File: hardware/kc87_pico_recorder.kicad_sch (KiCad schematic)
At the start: 8 parts, among them J1 DIN-5_180degree, U1 LM293P

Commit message: Refactor project structure: replace main.c with kc87_pico_recorder.c, update CMakeLists.txt, and add config.h for GPIO configuration
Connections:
- net KC87_REC_PICO: now also A1.4 (GPIO2); no longer A1.14 (GPIO10)
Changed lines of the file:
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@@
 	(wire
 		(pts
-			(xy 167.64 100.33) (xy 170.18 100.33)
+			(xy 166.37 80.01) (xy 170.18 80.01)
 		)
 		(stroke
@@
 	(global_label "KC87_REC_PICO"
 		(shape input)
-		(at 167.64 100.33 180)
+		(at 166.37 80.01 180)
 		(fields_autoplaced yes)
 		(effects
@@
 		)
 		(property "Intersheetrefs" "${INTERSHEET_REFS}"
-			(at 149.5963 100.33 0)
+			(at 148.3263 80.01 0)
 			(effects
 				(font

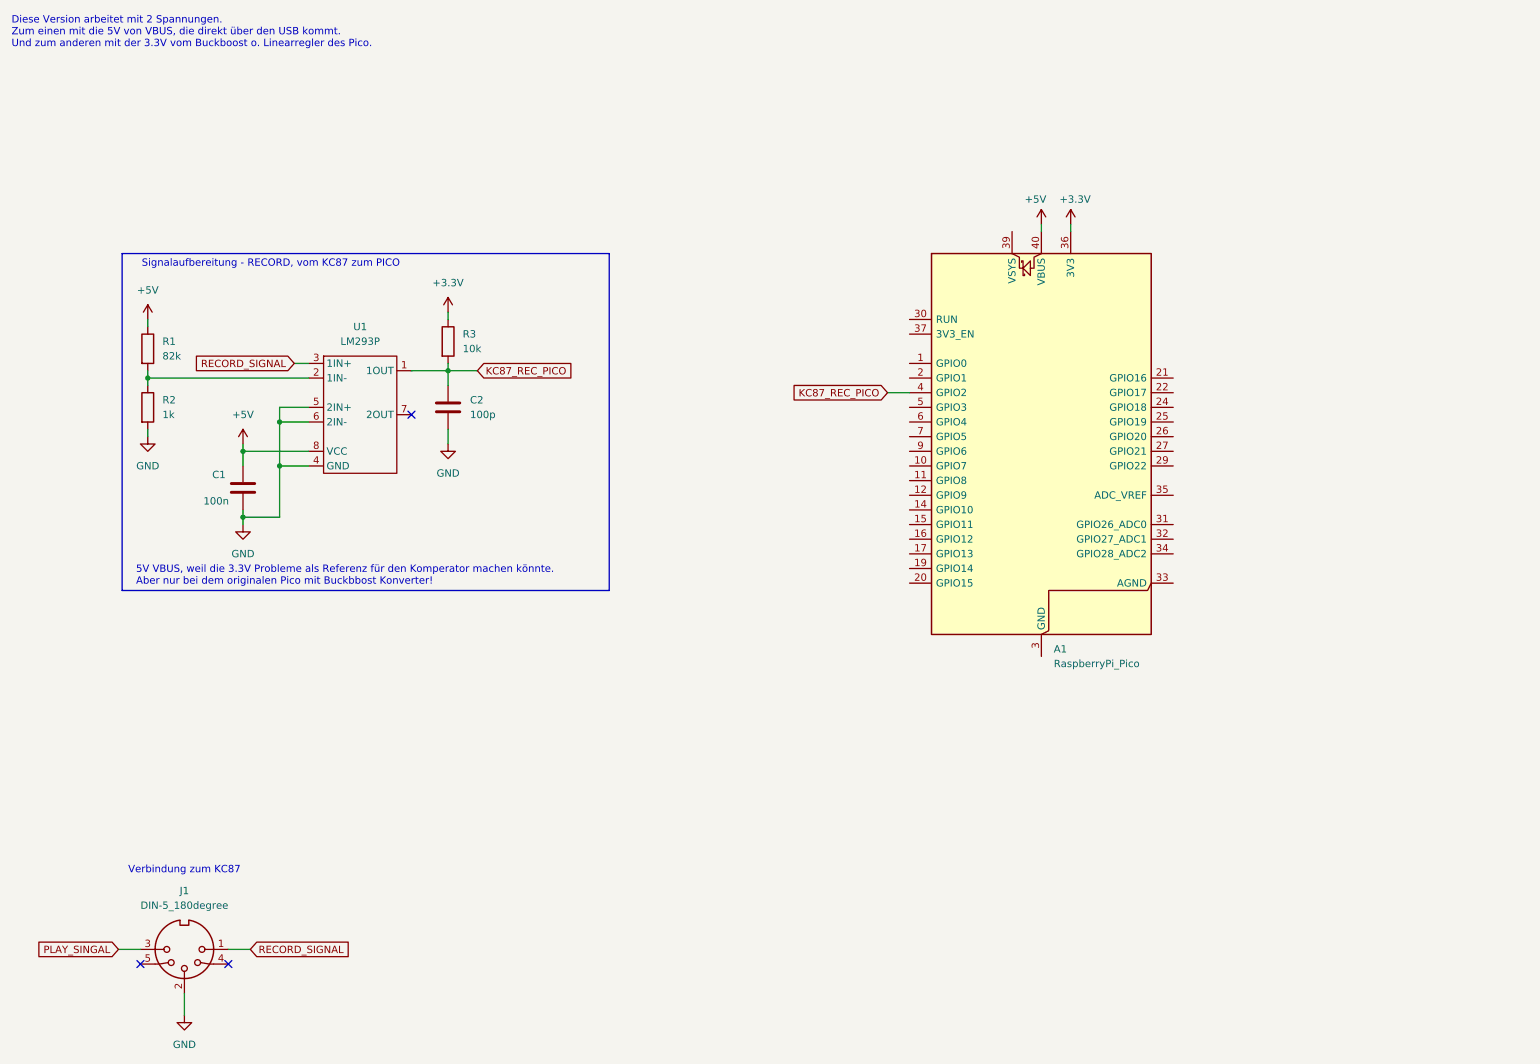
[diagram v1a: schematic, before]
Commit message: Hardware: change kc87_pico_recorder.kicad_sch (new amplifier)
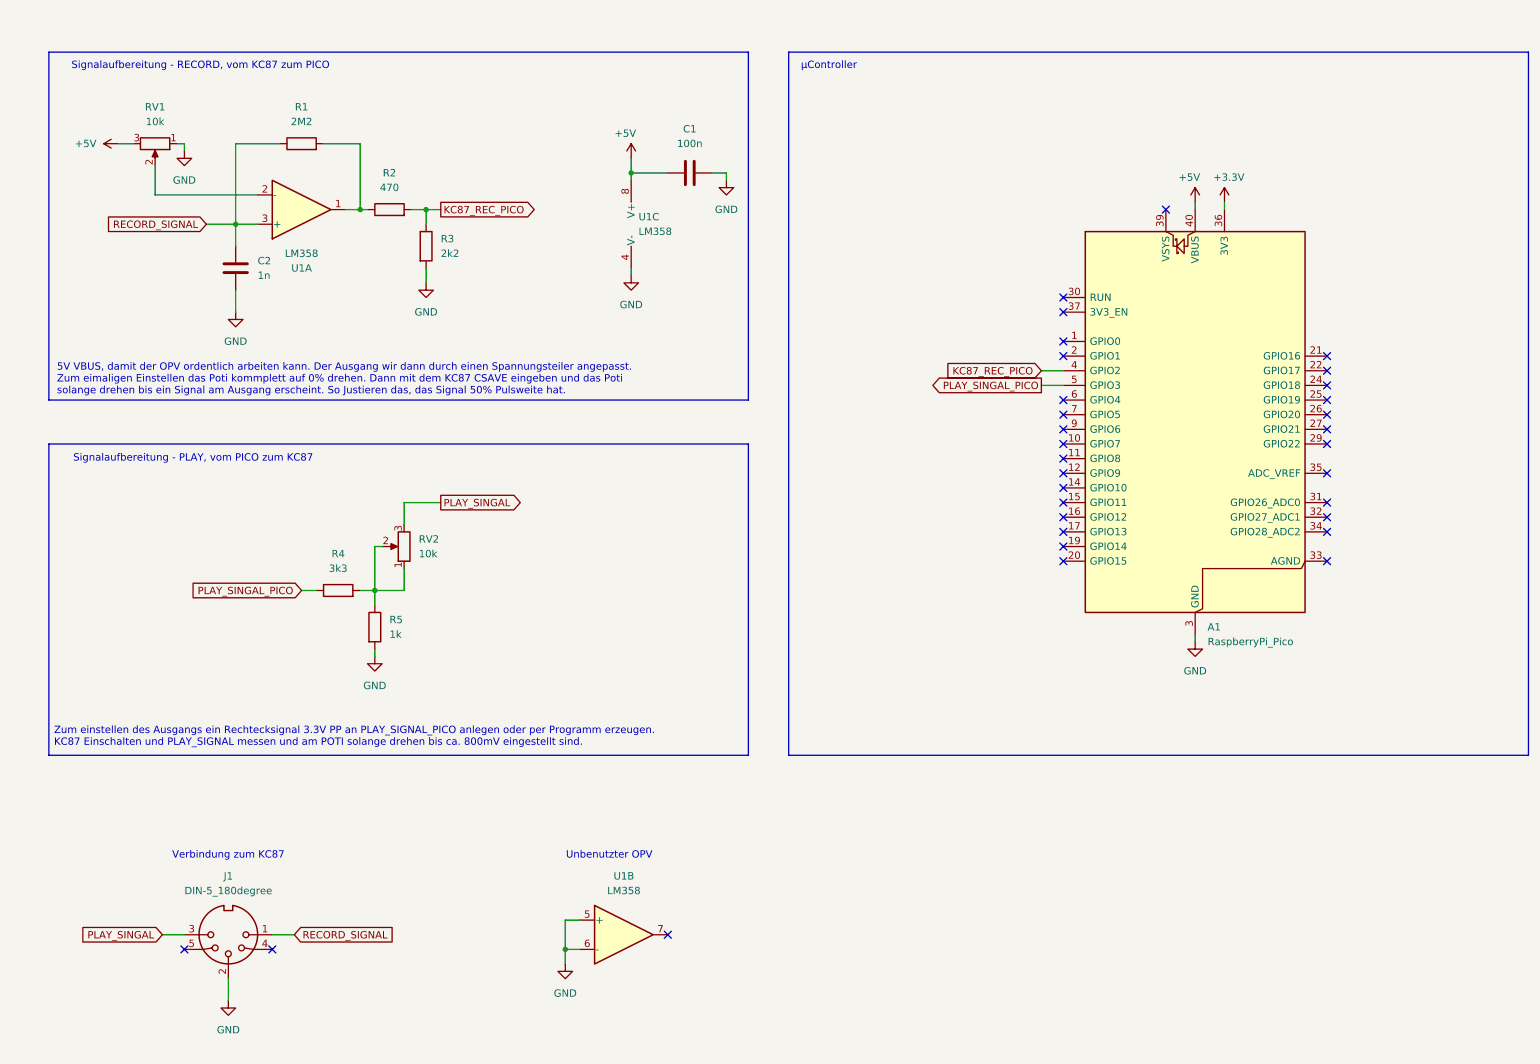
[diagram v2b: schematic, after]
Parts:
- removed U1: LM293P, Package_DIP:DIP-8_W7.62mm_SMDSocket_SmallPads, symbol ic_tk:LM293P
- added R4: 3k3, symbol Device:R
- added R5: 1k, symbol Device:R
- added RV1, RV2: 10k, symbol Device:R_Potentiometer
- added U1: LM358, symbol Amplifier_Operational:LM358
- C2: value 100p -> 1n; footprint Capacitor_SMD:C_0805_2012Metric_Pad1.18x1.45mm_HandSolder -> (none)
- R1: value 82k -> 2M2; footprint Resistor_SMD:R_0805_2012Metric_Pad1.20x1.40mm_HandSolder -> (none)
- R2: value 1k -> 470; footprint Resistor_SMD:R_0805_2012Metric_Pad1.20x1.40mm_HandSolder -> (none)
- R3: value 10k -> 2k2; footprint Resistor_SMD:R_0805_2012Metric_Pad1.20x1.40mm_HandSolder -> (none)
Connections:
- net +3.3V: no longer R3.1
- net +5V: now also RV1.3, U1.8 (V+); no longer R1.1
- net GND: now also A1.13 (GND), A1.18 (GND), A1.23 (GND), A1.28 (GND), A1.3 (GND), A1.38 (GND), A1.8 (GND), R3.2, R5.2, RV1.1, U1.4 (V-), U1.5 (+), U1.6 (-); no longer R2.2
- net KC87_REC_PICO: now also R2.2, R3.1; no longer C2.1, R3.2
- net PLAY_SINGAL: now also RV2.3
- net RECORD_SIGNAL: now also C2.1, R1.1, U1.3 (+)
- net at R1.2, R2.1: now also U1.1
- net PLAY_SINGAL_PICO: now reaches A1.5 (GPIO3)
- net PLAY_SINGAL_PICO: now also R4.1
- new net: R4.2, R5.1, RV2.1, RV2.2
- new net: RV1.2, U1.2 (-)
- no-connect marks 3 -> 32
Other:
- note added: "5V VBUS, damit der OPV ordentlich arbeiten kann. Der Ausgang wir dann durch einen Spannungsteiler angepasst. Zum eimaligen Einstellen das Poti kommplett auf 0% drehen. Dann mit dem KC87 CSAVE eingeben und das Poti solange drehen bis ein Signal am Ausgang erscheint. So Justieren das, das Signal 50% Pulsweite hat."
- note added: "Signalaufbereitung - PLAY, vom PICO zum KC87"
- note added: "Unbenutzter OPV"
- note added: "Zum einstellen des Ausgangs ein Rechtecksignal 3.3V PP an PLAY_SIGNAL_PICO anlegen oder per Programm erzeugen. KC87 Einschalten und PLAY_SIGNAL messen und am POTI solange drehen bis ca. 800mV eingestellt sind."
- note added: "µController"
- note removed: "5V VBUS, weil die 3.3V Probleme als Referenz für den Komperator machen könnte. Aber nur bei dem originalen Pico mit Buckbbost Konverter!"
- note removed: "Diese Version arbeitet mit 2 Spannungen. Zum einen mit die 5V von VBUS, die direkt über den USB kommt. Und zum anderen mit der 3.3V vom Buckboost o. Linearregler des Pico."
- moved on the sheet: A1, J1
